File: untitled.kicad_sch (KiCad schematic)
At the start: 71 parts, among them J4 Conn_01x08_Pin, SW1 SW_SPST, U1 MCP6L04T-E_SL, U2 Teensy4.1, U3 MCP6L04T-E_SL

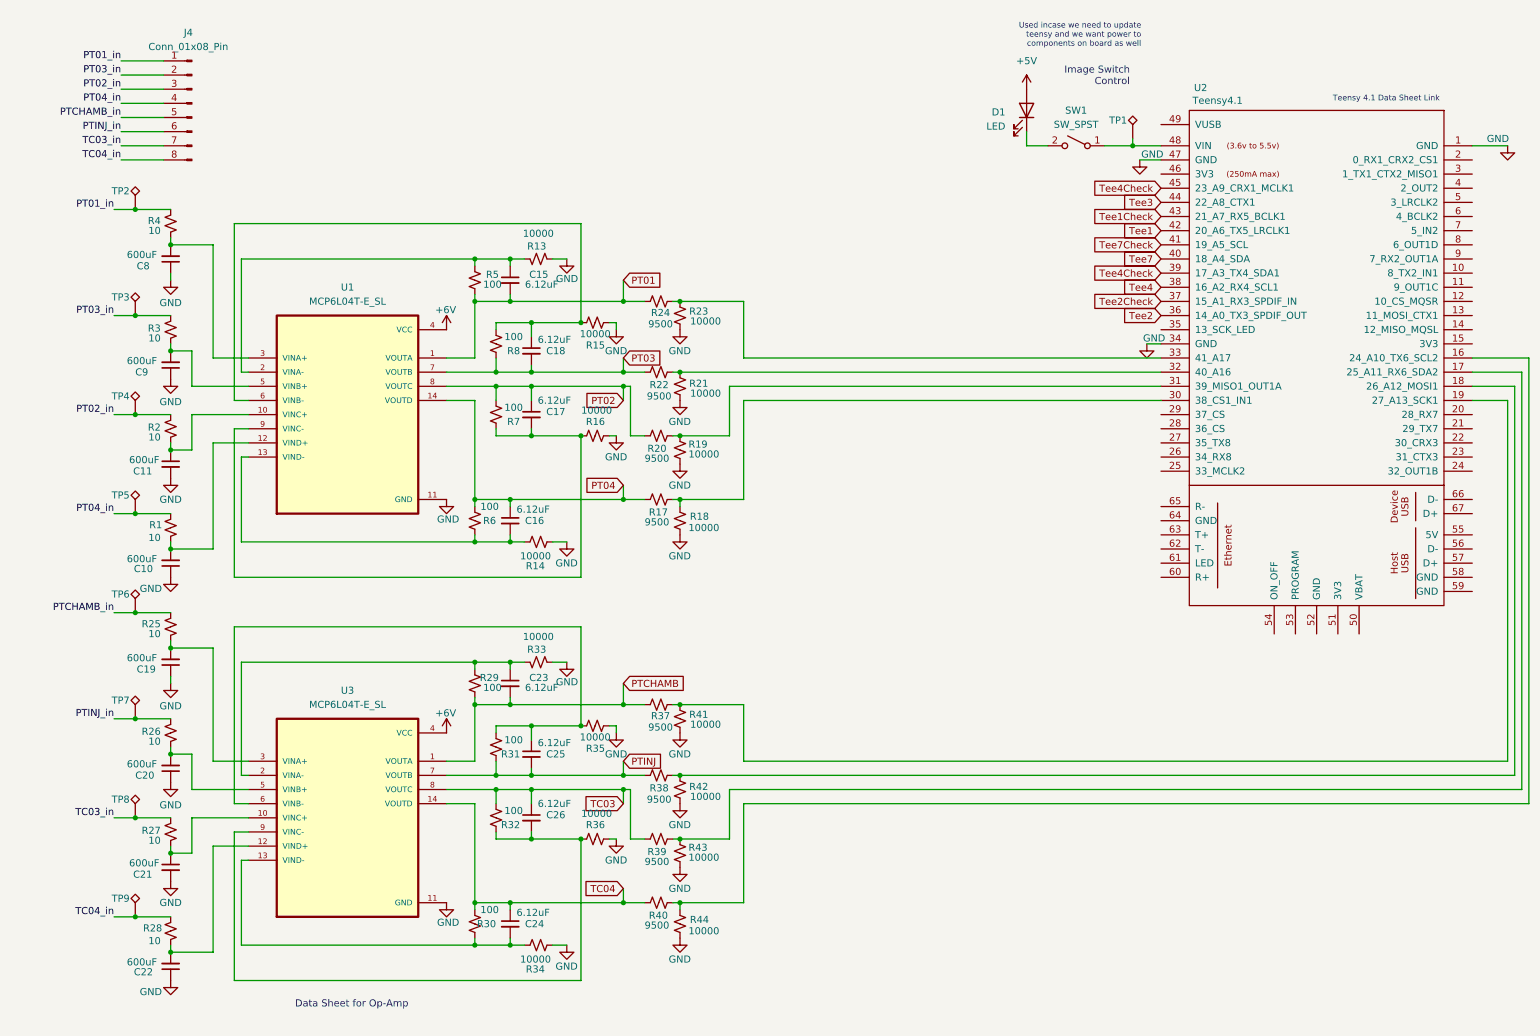
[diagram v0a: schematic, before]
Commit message: Purge Oscillator/Timer
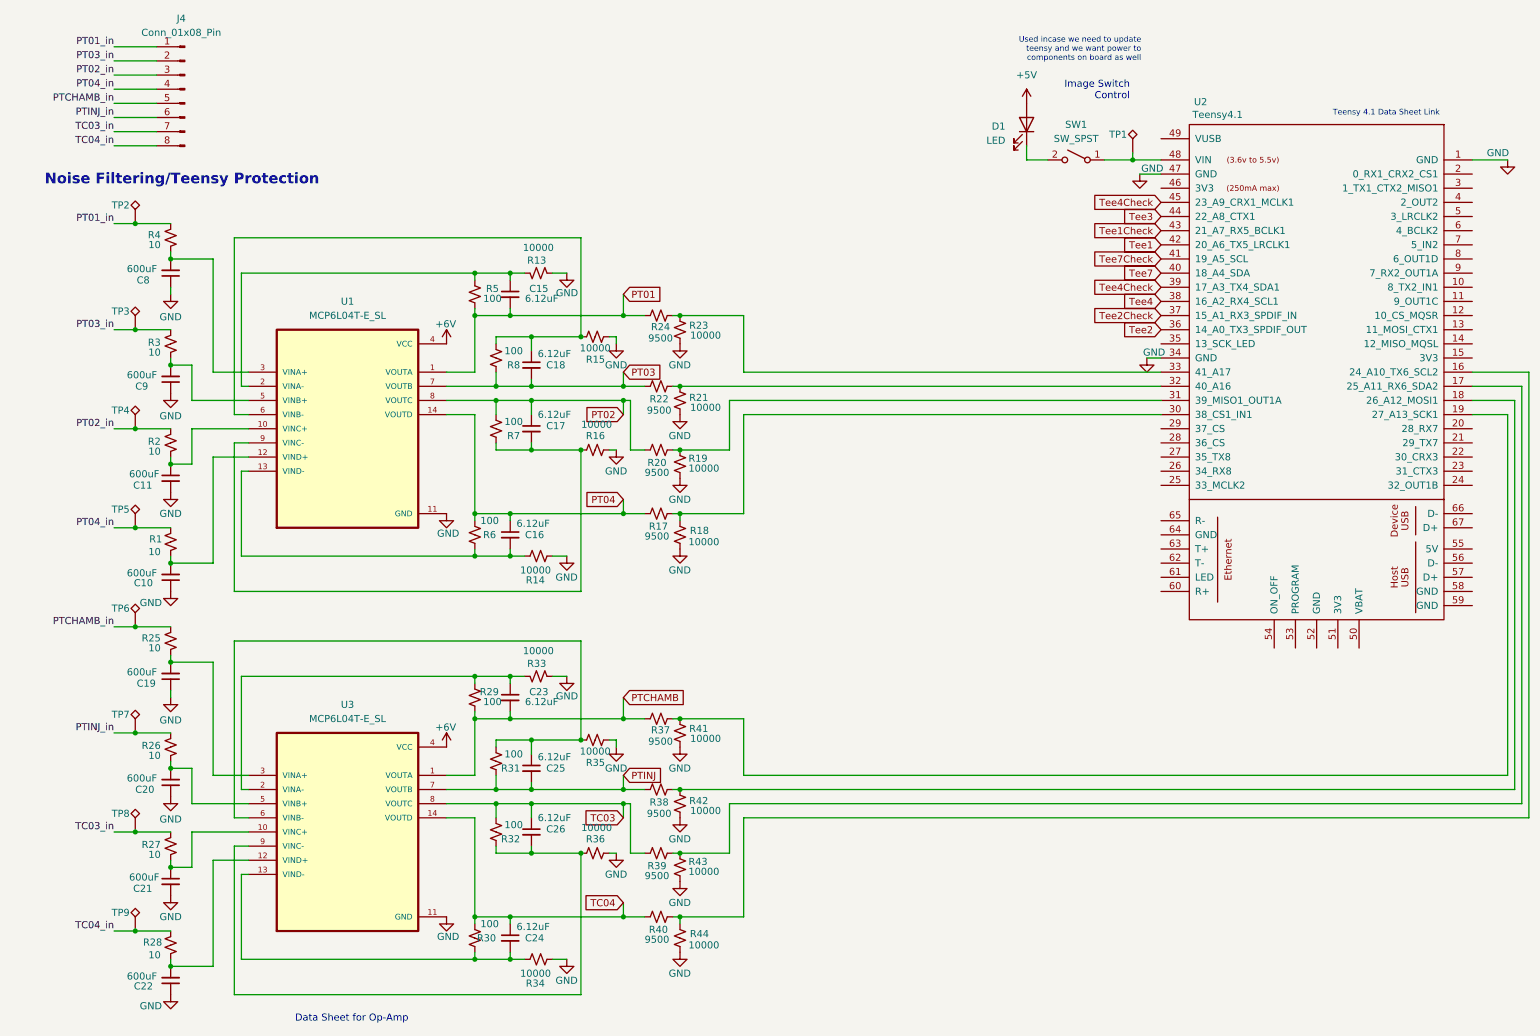
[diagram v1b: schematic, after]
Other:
- note added: "Noise Filtering/Teensy Protection"
- moved on the sheet: C10, C11, C15, C16, C17, C18, C19, C20, C21, C22, C23, C24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

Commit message: Voltage Fix, Tri-State Buffers, Double-Buffer
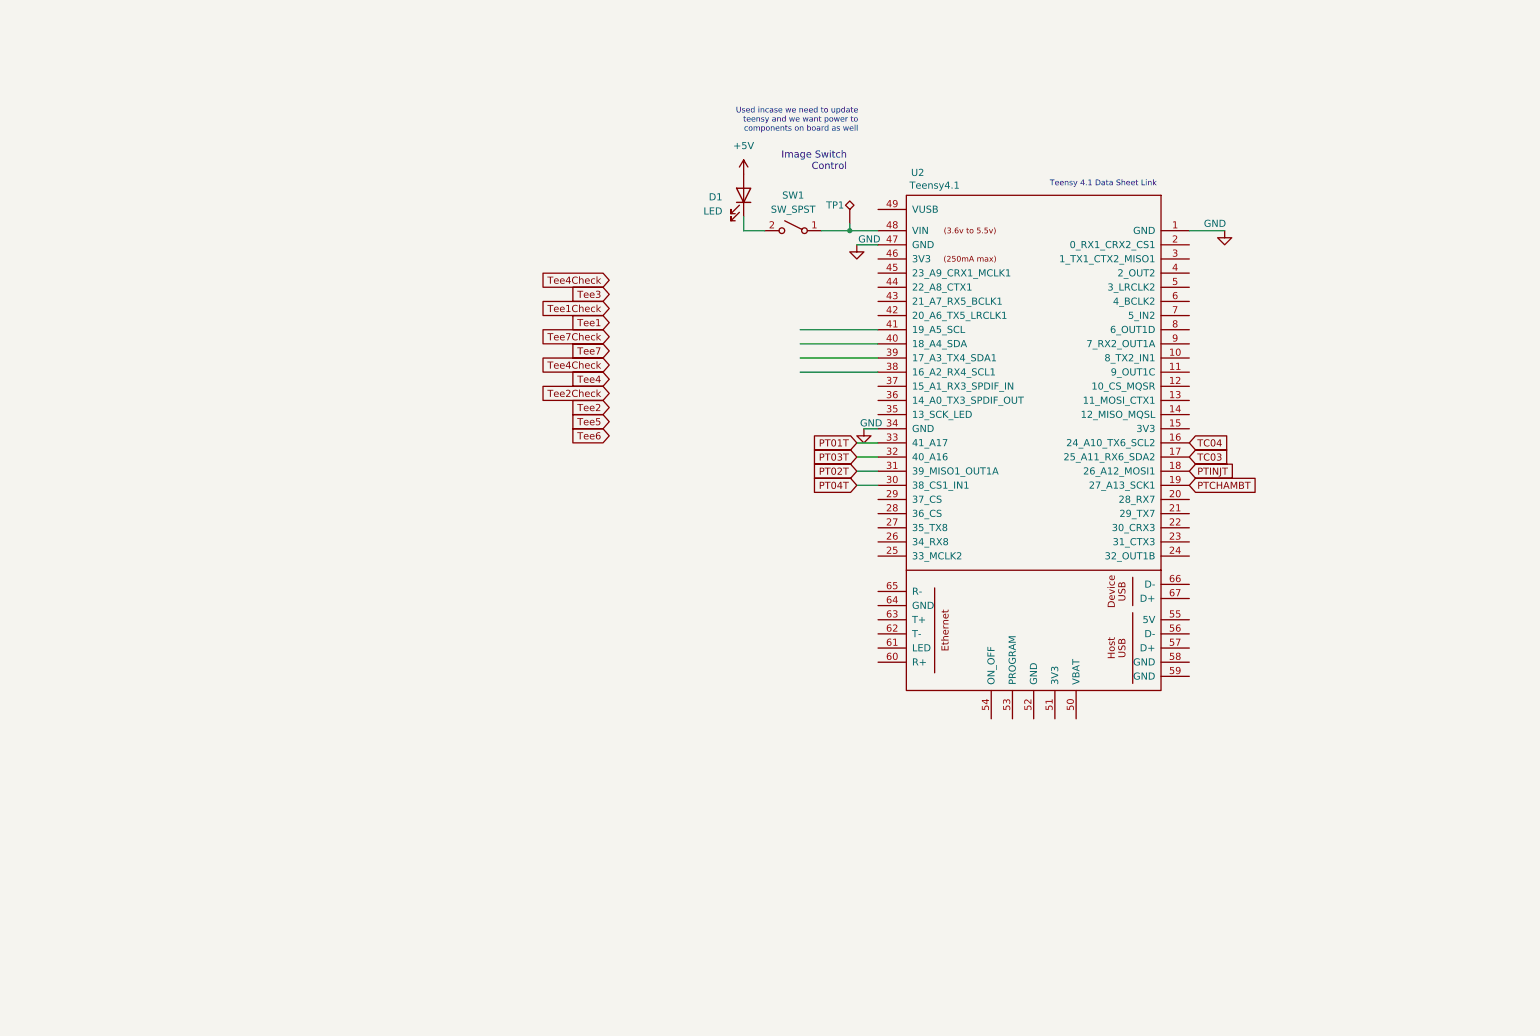
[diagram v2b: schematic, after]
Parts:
- removed C10, C11, C19, C20, C21, C22, C8, C9: 600uF, symbol Device:C_Small
- removed C15, C16, C17, C18, C23, C24, C25, C26: 6.12uF, symbol Device:C_Small
- removed J4: Conn_01x08_Pin, symbol Connector:Conn_01x08_Pin
- removed R1, R2, R25, R26, R27, R28, R3, R4: 10, symbol Device:R_Small_US
- removed R13, R14, R15, R16, R18, R19, R21, R23, R33, R34, R35, R36, R41, R42, R43, R44: 10000, symbol Device:R_Small_US
- removed R17, R20, R22, R24, R37, R38, R39, R40: 9500, symbol Device:R_Small_US
- removed R29, R30, R31, R32, R5, R6, R7, R8: 100, symbol Device:R_Small_US
- removed TP2, TP3, TP4, TP5, TP6, TP7, TP8, TP9: TestPoint_Alt, symbol Connector:TestPoint_Alt
- removed U1, U3: MCP6L04T-E_SL, MCP6L04T-E_SL:SOIC127P600X175-14N, symbol MCP6L04T-E_SL:MCP6L04T-E_SL
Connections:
- net TC03: now also U2.17 (25_A11_RX6_SDA2)
- net TC04: now also U2.16 (24_A10_TX6_SCL2)
- net Tee1: no longer U2.42 (20_A6_TX5_LRCLK1)
- net Tee1Check: no longer U2.43 (21_A7_RX5_BCLK1)
- net Tee2: no longer U2.36 (14_A0_TX3_SPDIF_OUT)
- net Tee2Check: no longer U2.37 (15_A1_RX3_SPDIF_IN)
- net Tee3: no longer U2.44 (22_A8_CTX1)
- net Tee4: no longer U2.38 (16_A2_RX4_SCL1)
- net Tee4Check: no longer U2.39 (17_A3_TX4_SDA1), U2.45 (23_A9_CRX1_MCLK1)
- net Tee7: no longer U2.40 (18_A4_SDA)
- net Tee7Check: no longer U2.41 (19_A5_SCL)
- net PTCHAMBT: now reaches U2.19 (27_A13_SCK1)
- net PT03T: now reaches U2.32 (40_A16)
- net PT02T: now reaches U2.31 (39_MISO1_OUT1A)
- net PT01T: now reaches U2.33 (41_A17)
- net PT04T: now reaches U2.30 (38_CS1_IN1)
- net PTINJT: now reaches U2.18 (26_A12_MOSI1)
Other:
- note removed: "Data Sheet for Op-Amp"
- note removed: "Noise Filtering/Teensy Protection"
- moved on the sheet: D1, SW1, TP1, U2
